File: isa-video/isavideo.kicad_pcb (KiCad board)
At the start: 4 copper layers, 106.4 x 95 mm, 142 parts, among them J1 PROG, J2 DB15_Female_HighDensity_Mount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, J3 PJRAN1X1U04X, J4 10029449-111RLF, J5 Conn_ISA_8bit, J6 RFMOD, J7 Conn_01x05, J8 Conn_02x06_Odd_Even, SW1 SW_DIP_x04, U1 ICE40HX4K-TQ144, U10 APX803S00-29SA-7, U11 74HCT125, U12 TFP410PAP, U2 SST26VF080A-104I/SN, U3 74ALVC164245, U4 74ALVC164245, U5 74ALVC164245, U6 ADA4891-3, U7 IS61WV5128BLL-10KLI, U8 LD1085D2T33R, U9 AP2114HA-1.2, X1 10MHz, X2 14.318MHz

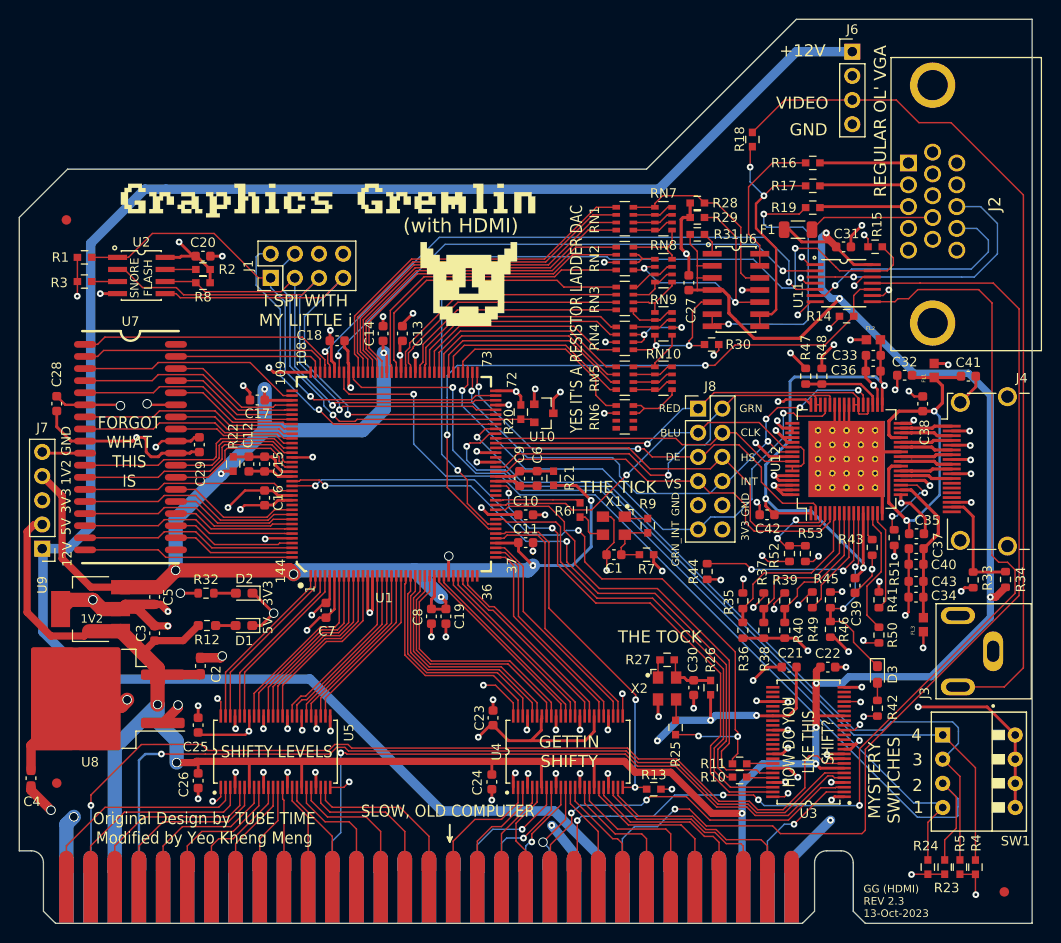
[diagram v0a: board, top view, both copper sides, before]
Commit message: clean up unused tracks
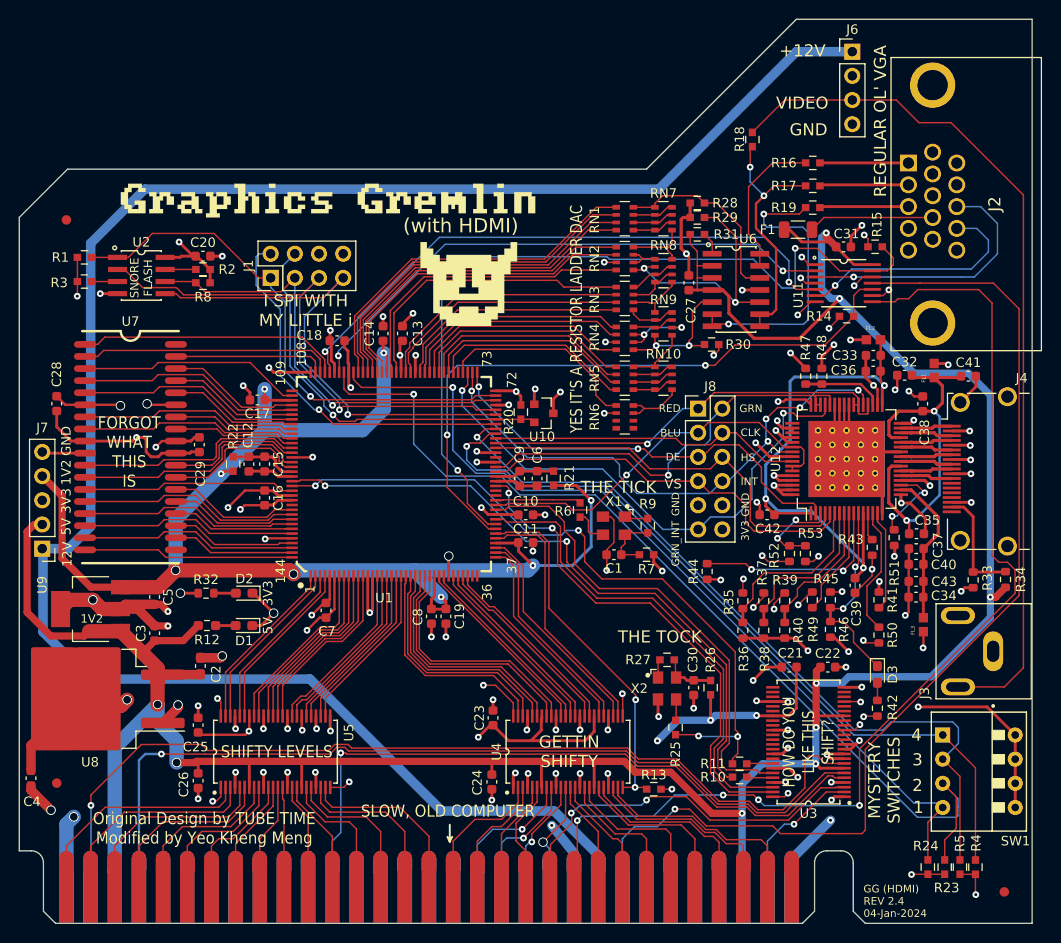
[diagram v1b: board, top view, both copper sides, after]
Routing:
- net /Bus Interface/~{IOW_5V}: track 24.5 -> 14.1 mm
- net /HDMI_GRN_INT: track 57.5 -> 56.9 mm
- net +5V: track 300.2 -> 299.6 mm
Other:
- board text added: "GG (HDMI) REV 2.4 04-Jan-2024"
- board text removed: "GG (HDMI) REV 2.3 13-Oct-2023"
